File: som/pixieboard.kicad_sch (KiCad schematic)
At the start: 5 parts, among them SW1 SW_DIP_x03, U1 XC7A200T-3FBG484E

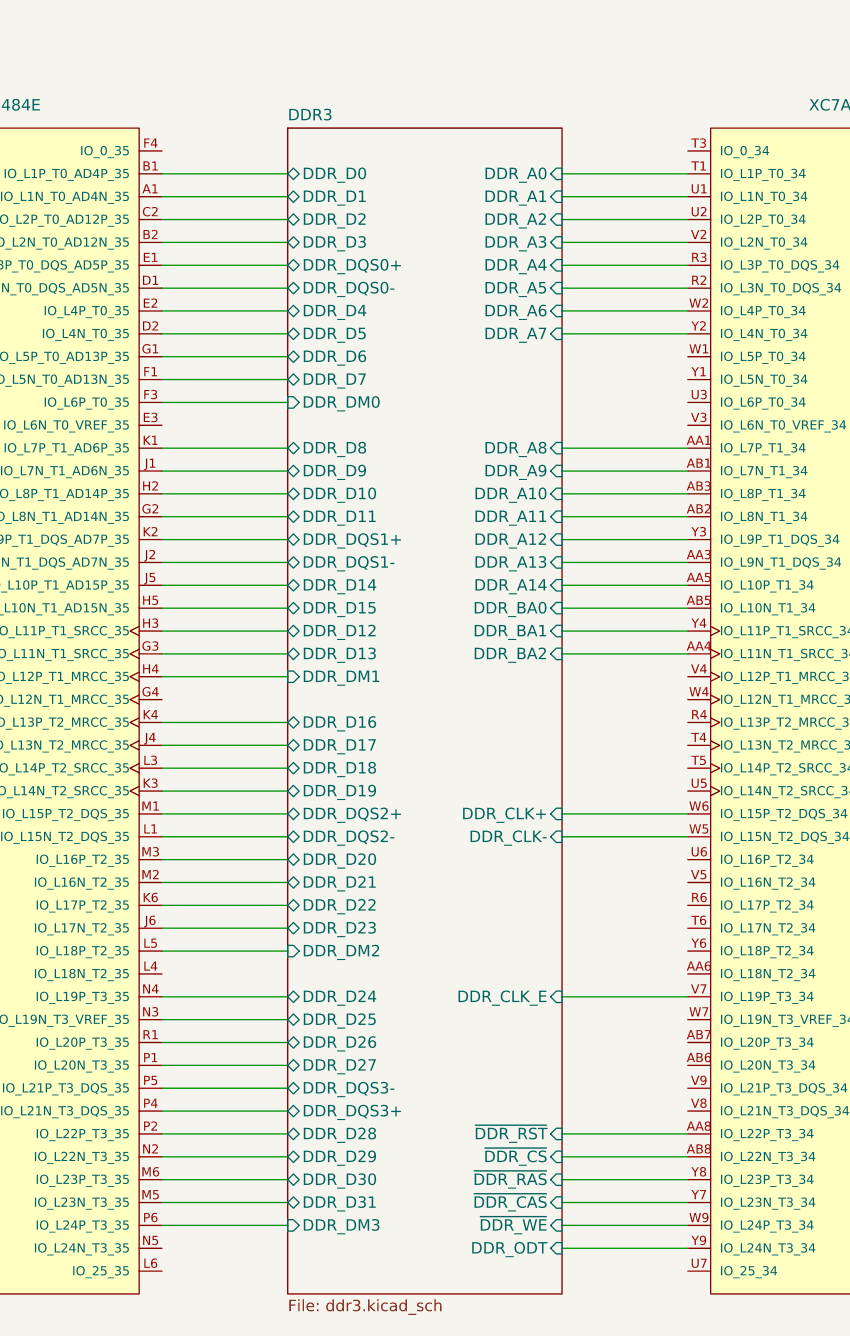
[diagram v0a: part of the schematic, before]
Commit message: Completed DDR3L routing
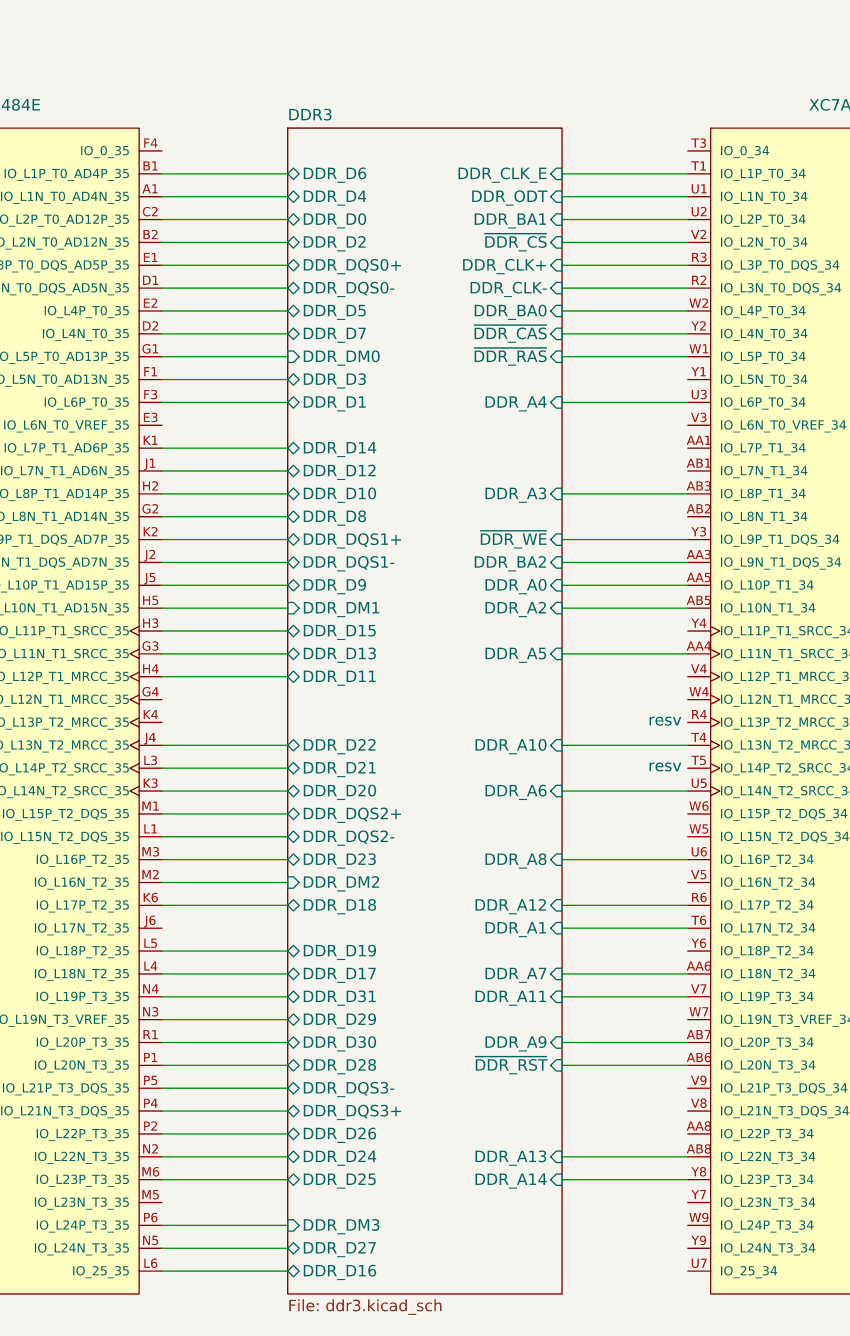
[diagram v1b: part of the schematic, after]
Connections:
- net DDR3/DDR_A0: now also U1.AA5 (IO_L10P_T1_34); no longer U1.T1 (IO_L1P_T0_34)
- net DDR3/DDR_A1: now also U1.T6 (IO_L17N_T2_34); no longer U1.U1 (IO_L1N_T0_34)
- net DDR3/DDR_A10: now also U1.T4 (IO_L13N_T2_MRCC_34); no longer U1.AB3 (IO_L8P_T1_34)
- net DDR3/DDR_A11: now also U1.V7 (IO_L19P_T3_34); no longer U1.AB2 (IO_L8N_T1_34)
- net DDR3/DDR_A12: now also U1.R6 (IO_L17P_T2_34); no longer U1.Y3 (IO_L9P_T1_DQS_34)
- net DDR3/DDR_A13: now also U1.AB8 (IO_L22N_T3_34); no longer U1.AA3 (IO_L9N_T1_DQS_34)
- net DDR3/DDR_A14: now also U1.Y8 (IO_L23P_T3_34); no longer U1.AA5 (IO_L10P_T1_34)
- net DDR3/DDR_A2: now also U1.AB5 (IO_L10N_T1_34); no longer U1.U2 (IO_L2P_T0_34)
- net DDR3/DDR_A3: now also U1.AB3 (IO_L8P_T1_34); no longer U1.V2 (IO_L2N_T0_34)
- net DDR3/DDR_A4: now also U1.U3 (IO_L6P_T0_34); no longer U1.R3 (IO_L3P_T0_DQS_34)
- net DDR3/DDR_A5: now also U1.AA4 (IO_L11N_T1_SRCC_34); no longer U1.R2 (IO_L3N_T0_DQS_34)
- net DDR3/DDR_A6: now also U1.U5 (IO_L14N_T2_SRCC_34); no longer U1.W2 (IO_L4P_T0_34)
- net DDR3/DDR_A7: now also U1.AA6 (IO_L18N_T2_34); no longer U1.Y2 (IO_L4N_T0_34)
- net DDR3/DDR_A8: now also U1.U6 (IO_L16P_T2_34); no longer U1.AA1 (IO_L7P_T1_34)
- net DDR3/DDR_A9: now also U1.AB7 (IO_L20P_T3_34); no longer U1.AB1 (IO_L7N_T1_34)
- net DDR3/DDR_BA0: now also U1.W2 (IO_L4P_T0_34); no longer U1.AB5 (IO_L10N_T1_34)
- net DDR3/DDR_BA1: now also U1.U2 (IO_L2P_T0_34); no longer U1.Y4 (IO_L11P_T1_SRCC_34)
- net DDR3/DDR_BA2: now also U1.AA3 (IO_L9N_T1_DQS_34); no longer U1.AA4 (IO_L11N_T1_SRCC_34)
- net DDR3/DDR_CLK+: now also U1.R3 (IO_L3P_T0_DQS_34); no longer U1.W6 (IO_L15P_T2_DQS_34)
- net DDR3/DDR_CLK-: now also U1.R2 (IO_L3N_T0_DQS_34); no longer U1.W5 (IO_L15N_T2_DQS_34)
- net DDR3/DDR_CLK_E: now also U1.T1 (IO_L1P_T0_34); no longer U1.V7 (IO_L19P_T3_34)
- net DDR3/DDR_D0: now also U1.C2 (IO_L2P_T0_AD12P_35); no longer U1.B1 (IO_L1P_T0_AD4P_35)
- net DDR3/DDR_D1: now also U1.F3 (IO_L6P_T0_35); no longer U1.A1 (IO_L1N_T0_AD4N_35)
- net DDR3/DDR_D11: now also U1.H4 (IO_L12P_T1_MRCC_35); no longer U1.G2 (IO_L8N_T1_AD14N_35)
- net DDR3/DDR_D12: now also U1.J1 (IO_L7N_T1_AD6N_35); no longer U1.H3 (IO_L11P_T1_SRCC_35)
- net DDR3/DDR_D14: now also U1.K1 (IO_L7P_T1_AD6P_35); no longer U1.J5 (IO_L10P_T1_AD15P_35)
- net DDR3/DDR_D15: now also U1.H3 (IO_L11P_T1_SRCC_35); no longer U1.H5 (IO_L10N_T1_AD15N_35)
- net DDR3/DDR_D16: now also U1.L6 (IO_25_35); no longer U1.K4 (IO_L13P_T2_MRCC_35)
- net DDR3/DDR_D17: now also U1.L4 (IO_L18N_T2_35); no longer U1.J4 (IO_L13N_T2_MRCC_35)
- net DDR3/DDR_D18: now also U1.K6 (IO_L17P_T2_35); no longer U1.L3 (IO_L14P_T2_SRCC_35)
- net DDR3/DDR_D19: now also U1.L5 (IO_L18P_T2_35); no longer U1.K3 (IO_L14N_T2_SRCC_35)
- net DDR3/DDR_D2: now also U1.B2 (IO_L2N_T0_AD12N_35); no longer U1.C2 (IO_L2P_T0_AD12P_35)
- net DDR3/DDR_D20: now also U1.K3 (IO_L14N_T2_SRCC_35); no longer U1.M3 (IO_L16P_T2_35)
- net DDR3/DDR_D21: now also U1.L3 (IO_L14P_T2_SRCC_35); no longer U1.M2 (IO_L16N_T2_35)
- net DDR3/DDR_D22: now also U1.J4 (IO_L13N_T2_MRCC_35); no longer U1.K6 (IO_L17P_T2_35)
- net DDR3/DDR_D23: now also U1.M3 (IO_L16P_T2_35); no longer U1.J6 (IO_L17N_T2_35)
- net DDR3/DDR_D24: now also U1.N2 (IO_L22N_T3_35); no longer U1.N4 (IO_L19P_T3_35)
- net DDR3/DDR_D25: now also U1.M6 (IO_L23P_T3_35); no longer U1.N3 (IO_L19N_T3_VREF_35)
- net DDR3/DDR_D26: now also U1.P2 (IO_L22P_T3_35); no longer U1.R1 (IO_L20P_T3_35)
- net DDR3/DDR_D27: now also U1.N5 (IO_L24N_T3_35); no longer U1.P1 (IO_L20N_T3_35)
- net DDR3/DDR_D28: now also U1.P1 (IO_L20N_T3_35); no longer U1.P2 (IO_L22P_T3_35)
- net DDR3/DDR_D29: now also U1.N3 (IO_L19N_T3_VREF_35); no longer U1.N2 (IO_L22N_T3_35)
- net DDR3/DDR_D3: now also U1.F1 (IO_L5N_T0_AD13N_35); no longer U1.B2 (IO_L2N_T0_AD12N_35)
- net DDR3/DDR_D30: now also U1.R1 (IO_L20P_T3_35); no longer U1.M6 (IO_L23P_T3_35)
- net DDR3/DDR_D31: now also U1.N4 (IO_L19P_T3_35); no longer U1.M5 (IO_L23N_T3_35)
- net DDR3/DDR_D4: now also U1.A1 (IO_L1N_T0_AD4N_35); no longer U1.E2 (IO_L4P_T0_35)
- net DDR3/DDR_D5: now also U1.E2 (IO_L4P_T0_35); no longer U1.D2 (IO_L4N_T0_35)
- net DDR3/DDR_D6: now also U1.B1 (IO_L1P_T0_AD4P_35); no longer U1.G1 (IO_L5P_T0_AD13P_35)
- net DDR3/DDR_D7: now also U1.D2 (IO_L4N_T0_35); no longer U1.F1 (IO_L5N_T0_AD13N_35)
- net DDR3/DDR_D8: now also U1.G2 (IO_L8N_T1_AD14N_35); no longer U1.K1 (IO_L7P_T1_AD6P_35)
- net DDR3/DDR_D9: now also U1.J5 (IO_L10P_T1_AD15P_35); no longer U1.J1 (IO_L7N_T1_AD6N_35)
- net DDR3/DDR_DM0: now also U1.G1 (IO_L5P_T0_AD13P_35); no longer U1.F3 (IO_L6P_T0_35)
- net DDR3/DDR_DM1: now also U1.H5 (IO_L10N_T1_AD15N_35); no longer U1.H4 (IO_L12P_T1_MRCC_35)
- net DDR3/DDR_DM2: now also U1.M2 (IO_L16N_T2_35); no longer U1.L5 (IO_L18P_T2_35)
- net DDR3/DDR_ODT: now also U1.U1 (IO_L1N_T0_34); no longer U1.Y9 (IO_L24N_T3_34)
- net DDR3/~{DDR_CAS}: now also U1.Y2 (IO_L4N_T0_34); no longer U1.Y7 (IO_L23N_T3_34)
- net DDR3/~{DDR_CS}: now also U1.V2 (IO_L2N_T0_34); no longer U1.AB8 (IO_L22N_T3_34)
- net DDR3/~{DDR_RAS}: now also U1.W1 (IO_L5P_T0_34); no longer U1.Y8 (IO_L23P_T3_34)
- net DDR3/~{DDR_RST}: now also U1.AB6 (IO_L20N_T3_34); no longer U1.AA8 (IO_L22P_T3_34)
- net DDR3/~{DDR_WE}: now also U1.Y3 (IO_L9P_T1_DQS_34); no longer U1.W9 (IO_L24P_T3_34)
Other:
- note added: "resv"

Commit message: Mezz Power Tweak Ok
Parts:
- added H1, H2, H3, H4: MountingHole_Pad, MountingHole:MountingHole_2.2mm_M2_DIN965_Pad, symbol Mechanical:MountingHole_Pad
- added J1, J2, J3, J4: Conn_02x20_Counter_Clockwise, Mezzanine:Mezz_02x20_p0.5mm_M, symbol Connector_Generic:Conn_02x20_Counter_Clockwise
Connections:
- net GND: now also H1.1, H2.1, H3.1, H4.1

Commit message: Le DDR3 control traces
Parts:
- added C33: 100nF, Capacitor_SMD:C_0402_1005Metric, symbol Device:C_Small
- added J5, J6: Conn_02x20_Counter_Clockwise, Mezzanine:Mezz_02x20_p0.5mm_M, symbol Connector_Generic:Conn_02x20_Counter_Clockwise
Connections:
- net +3V3: now also C33.1
- net DDR3/DDR_A1: now also U1.V5 (IO_L16N_T2_34); no longer U1.T6 (IO_L17N_T2_34)
- net DDR3/DDR_A10: now also U1.T6 (IO_L17N_T2_34); no longer U1.T4 (IO_L13N_T2_MRCC_34)
- net DDR3/DDR_A11: now also U1.W6 (IO_L15P_T2_DQS_34); no longer U1.V7 (IO_L19P_T3_34)
- net DDR3/DDR_A12: now also U1.V4 (IO_L12P_T1_MRCC_34); no longer U1.R6 (IO_L17P_T2_34)
- net DDR3/DDR_A14: now also U1.W7 (IO_L19N_T3_VREF_34); no longer U1.Y8 (IO_L23P_T3_34)
- net DDR3/DDR_A2: now also U1.AA6 (IO_L18N_T2_34); no longer U1.AB5 (IO_L10N_T1_34)
- net DDR3/DDR_A3: now also U1.AA4 (IO_L11N_T1_SRCC_34); no longer U1.AB3 (IO_L8P_T1_34)
- net DDR3/DDR_A4: now also U1.T4 (IO_L13N_T2_MRCC_34); no longer U1.U3 (IO_L6P_T0_34)
- net DDR3/DDR_A5: now also U1.AB5 (IO_L10N_T1_34); no longer U1.AA4 (IO_L11N_T1_SRCC_34)
- net DDR3/DDR_A7: now also U1.AB6 (IO_L20N_T3_34); no longer U1.AA6 (IO_L18N_T2_34)
- net DDR3/DDR_A9: now also U1.Y7 (IO_L23N_T3_34); no longer U1.AB7 (IO_L20P_T3_34)
- net DDR3/DDR_BA0: now also U1.AA3 (IO_L9N_T1_DQS_34); no longer U1.W2 (IO_L4P_T0_34)
- net DDR3/DDR_BA1: now also U1.W2 (IO_L4P_T0_34); no longer U1.U2 (IO_L2P_T0_34)
- net DDR3/DDR_BA2: now also U1.Y4 (IO_L11P_T1_SRCC_34); no longer U1.AA3 (IO_L9N_T1_DQS_34)
- net DDR3/DDR_CLK_E: now also U1.R6 (IO_L17P_T2_34); no longer U1.T1 (IO_L1P_T0_34)
- net DDR3/~{DDR_CAS}: now also U1.U2 (IO_L2P_T0_34); no longer U1.Y2 (IO_L4N_T0_34)
- net DDR3/~{DDR_RAS}: now also U1.T1 (IO_L1P_T0_34); no longer U1.W1 (IO_L5P_T0_34)
- net DDR3/~{DDR_RST}: now also U1.AB7 (IO_L20P_T3_34); no longer U1.AB6 (IO_L20N_T3_34)
- net GND: now also C33.2
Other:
- moved on the sheet: U1G

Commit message: ok
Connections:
- net DDR3/DDR_A0: no longer U1.AA5 (IO_L10P_T1_34)
- net DDR3/DDR_A1: no longer U1.V5 (IO_L16N_T2_34)
- net DDR3/DDR_A10: now also U1.U3 (IO_L6P_T0_34); no longer U1.T6 (IO_L17N_T2_34)
- net DDR3/DDR_A11: no longer U1.W6 (IO_L15P_T2_DQS_34)
- net DDR3/DDR_A13: no longer U1.AB8 (IO_L22N_T3_34)
- net DDR3/DDR_A14: no longer U1.W7 (IO_L19N_T3_VREF_34)
- net DDR3/DDR_A2: no longer U1.AA6 (IO_L18N_T2_34)
- net DDR3/DDR_A3: no longer U1.AA4 (IO_L11N_T1_SRCC_34)
- net DDR3/DDR_A4: now also U1.Y6 (IO_L18P_T2_34); no longer U1.T4 (IO_L13N_T2_MRCC_34)
- net DDR3/DDR_A5: no longer U1.AB5 (IO_L10N_T1_34)
- net DDR3/DDR_A6: now also U1.AA6 (IO_L18N_T2_34); no longer U1.U5 (IO_L14N_T2_SRCC_34)
- net DDR3/DDR_A7: no longer U1.AB6 (IO_L20N_T3_34)
- net DDR3/DDR_A8: now also U1.AB7 (IO_L20P_T3_34); no longer U1.U6 (IO_L16P_T2_34)
- net DDR3/DDR_A9: no longer U1.Y7 (IO_L23N_T3_34)
- net DDR3/DDR_BA0: no longer U1.AA3 (IO_L9N_T1_DQS_34)
- net DDR3/DDR_BA1: now also U1.W5 (IO_L15N_T2_DQS_34); no longer U1.W2 (IO_L4P_T0_34)
- net DDR3/DDR_BA2: no longer U1.Y4 (IO_L11P_T1_SRCC_34)
- net DDR3/DDR_CLK+: now also U1.T1 (IO_L1P_T0_34); no longer U1.R3 (IO_L3P_T0_DQS_34)
- net DDR3/DDR_CLK-: now also U1.U1 (IO_L1N_T0_34); no longer U1.R2 (IO_L3N_T0_DQS_34)
- net DDR3/DDR_CLK_E: now also U1.U2 (IO_L2P_T0_34); no longer U1.R6 (IO_L17P_T2_34)
- net DDR3/DDR_ODT: no longer U1.U1 (IO_L1N_T0_34)
- net DDR3/~{DDR_CAS}: no longer U1.U2 (IO_L2P_T0_34)
- net DDR3/~{DDR_CS}: no longer U1.V2 (IO_L2N_T0_34)
- net DDR3/~{DDR_RAS}: no longer U1.T1 (IO_L1P_T0_34)
- net DDR3/~{DDR_RST}: no longer U1.AB7 (IO_L20P_T3_34)
- net DDR3/~{DDR_WE}: no longer U1.Y3 (IO_L9P_T1_DQS_34)

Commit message: DDR3 (again)
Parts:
- added C53, C54, C55, C56: 1nF, Capacitor_SMD:C_0402_1005Metric, symbol Device:C_Small
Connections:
- net DDR3/DDR_A0: now also U1.W5 (IO_L15N_T2_DQS_34)
- net DDR3/DDR_A1: now also U1.W4 (IO_L12N_T1_MRCC_34)
- net DDR3/DDR_A10: now also U1.R6 (IO_L17P_T2_34); no longer U1.U3 (IO_L6P_T0_34)
- net DDR3/DDR_A11: now also U1.Y6 (IO_L18P_T2_34)
- net DDR3/DDR_A12: now also U1.T6 (IO_L17N_T2_34); no longer U1.V4 (IO_L12P_T1_MRCC_34)
- net DDR3/DDR_A13: now also U1.AB6 (IO_L20N_T3_34)
- net DDR3/DDR_A14: now also U1.AB7 (IO_L20P_T3_34)
- net DDR3/DDR_A2: now also U1.AA5 (IO_L10P_T1_34)
- net DDR3/DDR_A3: now also U1.Y3 (IO_L9P_T1_DQS_34)
- net DDR3/DDR_A4: now also U1.V7 (IO_L19P_T3_34); no longer U1.Y6 (IO_L18P_T2_34)
- net DDR3/DDR_A5: now also U1.Y4 (IO_L11P_T1_SRCC_34)
- net DDR3/DDR_A6: now also U1.Y7 (IO_L23N_T3_34); no longer U1.AA6 (IO_L18N_T2_34)
- net DDR3/DDR_A7: now also U1.AA4 (IO_L11N_T1_SRCC_34)
- net DDR3/DDR_A8: now also U1.AA8 (IO_L22P_T3_34); no longer U1.AB7 (IO_L20P_T3_34)
- net DDR3/DDR_A9: now also U1.AB5 (IO_L10N_T1_34)
- net DDR3/DDR_BA0: now also U1.Y2 (IO_L4N_T0_34)
- net DDR3/DDR_BA1: now also U1.U6 (IO_L16P_T2_34); no longer U1.W5 (IO_L15N_T2_DQS_34)
- net DDR3/DDR_BA2: now also U1.V4 (IO_L12P_T1_MRCC_34)
- net DDR3/DDR_CLK_E: now also U1.R3 (IO_L3P_T0_DQS_34); no longer U1.U2 (IO_L2P_T0_34)
- net DDR3/DDR_D1: now also U1.G1 (IO_L5P_T0_AD13P_35); no longer U1.F3 (IO_L6P_T0_35)
- net DDR3/DDR_D10: now also U1.K1 (IO_L7P_T1_AD6P_35); no longer U1.H2 (IO_L8P_T1_AD14P_35)
- net DDR3/DDR_D11: now also U1.G3 (IO_L11N_T1_SRCC_35); no longer U1.H4 (IO_L12P_T1_MRCC_35)
- net DDR3/DDR_D12: now also U1.H4 (IO_L12P_T1_MRCC_35); no longer U1.J1 (IO_L7N_T1_AD6N_35)
- net DDR3/DDR_D13: now also U1.H5 (IO_L10N_T1_AD15N_35); no longer U1.G3 (IO_L11N_T1_SRCC_35)
- net DDR3/DDR_D14: now also U1.H2 (IO_L8P_T1_AD14P_35); no longer U1.K1 (IO_L7P_T1_AD6P_35)
- net DDR3/DDR_D15: now also U1.G4 (IO_L12N_T1_MRCC_35); no longer U1.H3 (IO_L11P_T1_SRCC_35)
- net DDR3/DDR_D16: now also U1.M2 (IO_L16N_T2_35); no longer U1.L6 (IO_25_35)
- net DDR3/DDR_D18: now also U1.L3 (IO_L14P_T2_SRCC_35); no longer U1.K6 (IO_L17P_T2_35)
- net DDR3/DDR_D2: now also U1.B1 (IO_L1P_T0_AD4P_35); no longer U1.B2 (IO_L2N_T0_AD12N_35)
- net DDR3/DDR_D20: now also U1.J4 (IO_L13N_T2_MRCC_35); no longer U1.K3 (IO_L14N_T2_SRCC_35)
- net DDR3/DDR_D21: now also U1.M3 (IO_L16P_T2_35); no longer U1.L3 (IO_L14P_T2_SRCC_35)
- net DDR3/DDR_D22: now also U1.K3 (IO_L14N_T2_SRCC_35); no longer U1.J4 (IO_L13N_T2_MRCC_35)
- net DDR3/DDR_D23: now also U1.K4 (IO_L13P_T2_MRCC_35); no longer U1.M3 (IO_L16P_T2_35)
- net DDR3/DDR_D24: now also U1.P2 (IO_L22P_T3_35); no longer U1.N2 (IO_L22N_T3_35)
- net DDR3/DDR_D25: now also U1.N2 (IO_L22N_T3_35); no longer U1.M6 (IO_L23P_T3_35)
- net DDR3/DDR_D26: now also U1.R1 (IO_L20P_T3_35); no longer U1.P2 (IO_L22P_T3_35)
- net DDR3/DDR_D27: now also U1.N4 (IO_L19P_T3_35); no longer U1.N5 (IO_L24N_T3_35)
- net DDR3/DDR_D28: now also U1.M6 (IO_L23P_T3_35); no longer U1.P1 (IO_L20N_T3_35)
- net DDR3/DDR_D29: now also U1.P1 (IO_L20N_T3_35); no longer U1.N3 (IO_L19N_T3_VREF_35)
- net DDR3/DDR_D3: now also U1.F3 (IO_L6P_T0_35); no longer U1.F1 (IO_L5N_T0_AD13N_35)
- net DDR3/DDR_D30: now also U1.P6 (IO_L24P_T3_35); no longer U1.R1 (IO_L20P_T3_35)
- net DDR3/DDR_D31: now also U1.N5 (IO_L24N_T3_35); no longer U1.N4 (IO_L19P_T3_35)
- net DDR3/DDR_D5: now also U1.F1 (IO_L5N_T0_AD13N_35); no longer U1.E2 (IO_L4P_T0_35)
- net DDR3/DDR_D6: now also U1.B2 (IO_L2N_T0_AD12N_35); no longer U1.B1 (IO_L1P_T0_AD4P_35)
- net DDR3/DDR_D8: now also U1.J1 (IO_L7N_T1_AD6N_35); no longer U1.G2 (IO_L8N_T1_AD14N_35)
- net DDR3/DDR_D9: now also U1.H3 (IO_L11P_T1_SRCC_35); no longer U1.J5 (IO_L10P_T1_AD15P_35)
- net DDR3/DDR_DM0: now also U1.E2 (IO_L4P_T0_35); no longer U1.G1 (IO_L5P_T0_AD13P_35)
- net DDR3/DDR_DM1: now also U1.G2 (IO_L8N_T1_AD14N_35); no longer U1.H5 (IO_L10N_T1_AD15N_35)
- net DDR3/DDR_DM2: now also U1.K6 (IO_L17P_T2_35); no longer U1.M2 (IO_L16N_T2_35)
- net DDR3/DDR_DM3: now also U1.M5 (IO_L23N_T3_35); no longer U1.P6 (IO_L24P_T3_35)
- net DDR3/DDR_ODT: now also U1.W1 (IO_L5P_T0_34)
- net DDR3/~{DDR_CAS}: now also U1.U3 (IO_L6P_T0_34)
- net DDR3/~{DDR_CS}: now also U1.W2 (IO_L4P_T0_34)
- net DDR3/~{DDR_RAS}: now also U1.U2 (IO_L2P_T0_34)
- net DDR3/~{DDR_WE}: now also U1.V2 (IO_L2N_T0_34)
- net GND: now also C53.2, C54.2, C55.2, C56.2
- net DDR_VREF: now reaches U1.V3 (IO_L6N_T0_VREF_34)
- net DDR_VREF: now also U1.E3 (IO_L6N_T0_VREF_35), U1.N3 (IO_L19N_T3_VREF_35), U1.W7 (IO_L19N_T3_VREF_34), C53.1, C54.1, C55.1, C56.1
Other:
- sheet DDR3 ports: added DDR_VREF; removed none
- note added: "Power rail summary: - 3.3 v 5.0 A input - 1.8 v 1.0 A output - 1.35 v 1.0 A output - 1.2 v 1.0 A output - 1.0 v 10.0 A local"

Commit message: I really should commit when I make it and not a month later
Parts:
- added C57: 100nF, Capacitor_SMD:C_0402_1005Metric, symbol Device:C_Small
- added U4: W25Q128JVS, Package_SO:SOIC-8_5.23x5.23mm_P1.27mm, symbol Memory_Flash:W25Q128JVS
- J1, J2, J3, J4, J5, J6: footprint Mezzanine:Mezz_02x20_p0.5mm_M -> Mezzanine:YXT-BB10-40P-02
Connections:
- net +3V3: now also C57.1, U4.8 (VCC)
- net GND: now also J1.35 (Pin_35), J1.36 (Pin_36), J1.37 (Pin_37), J1.4 (Pin_4), J1.5 (Pin_5), J1.6 (Pin_6), U1.L9 (VREFN_0), U1.M10 (VREFP_0), C57.2, U4.4 (GND)
- net QPI_CCLK: now also U4.6 (CLK)
- net QPI_CS: now also U4.1 (~{CS})
- net QPI_D0: now also U4.5 (DI(IO0))
- net QPI_D1: now also U4.2 (DO(IO1))
- net QPI_D2: now also U4.3 (IO2)
- net QPI_D3: now also U4.7 (IO3)
- net +5V: now reaches J1.1 (Pin_1)
- net +5V: now also J1.2 (Pin_2), J1.3 (Pin_3), J1.38 (Pin_38), J1.39 (Pin_39), J1.40 (Pin_40)
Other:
- sheet Power ports: added P_{GOOD}, V_{in}; removed none
- note removed: "Power rail summary: - 3.3 v 5.0 A input - 1.8 v 1.0 A output - 1.35 v 1.0 A output - 1.2 v 1.0 A output - 1.0 v 10.0 A local"
- moved on the sheet: J1

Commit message: ok
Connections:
- net +3V3: now also J1.33 (Pin_33), J1.34 (Pin_34), J1.7 (Pin_7), J1.8 (Pin_8)
- net GND: now also J1.32 (Pin_32), J1.9 (Pin_9)

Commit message: Work on GTP and power supplies for it
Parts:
- added R19: 240R, Resistor_SMD:R_0402_1005Metric, symbol Device:R_Small
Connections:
- net GND: now also J1.11 (Pin_11), J1.14 (Pin_14), J1.17 (Pin_17), J1.20 (Pin_20), J1.21 (Pin_21), J1.24 (Pin_24), J1.27 (Pin_27), J1.30 (Pin_30), J2.1 (Pin_1), J2.10 (Pin_10), J2.13 (Pin_13), J2.16 (Pin_16), J2.19 (Pin_19), J2.20 (Pin_20), J2.21 (Pin_21), J2.22 (Pin_22), J2.25 (Pin_25), J2.28 (Pin_28), J2.31 (Pin_31), J2.34 (Pin_34), J2.37 (Pin_37), J2.4 (Pin_4), J2.40 (Pin_40), J2.7 (Pin_7); no longer J1.32 (Pin_32), J1.9 (Pin_9)
- net MGT_TX0-: now reaches J1.10 (Pin_10)
- net MGT_TX0-: now also J1.31 (Pin_31), U1.A4 (MGTPTXN0_216)
- net MGT_TX1+: now reaches J1.12 (Pin_12)
- net MGT_TX1+: now also J1.29 (Pin_29), U1.D5 (MGTPTXP1_216)
- net MGT_TX1-: now reaches J1.13 (Pin_13)
- net MGT_TX1-: now also J1.28 (Pin_28), U1.C5 (MGTPTXN1_216)
- net MGT_TX2+: now reaches J1.15 (Pin_15)
- net MGT_TX2+: now also J1.26 (Pin_26), U1.B6 (MGTPTXP2_216)
- net MGT_TX2-: now reaches J1.16 (Pin_16)
- net MGT_TX2-: now also J1.25 (Pin_25), U1.A6 (MGTPTXN2_216)
- net MGT_TX3+: now reaches J1.18 (Pin_18)
- net MGT_TX3+: now also J1.23 (Pin_23), U1.D7 (MGTPTXP3_216)
- net MGT_TX3-: now reaches J1.19 (Pin_19)
- net MGT_TX3-: now also J1.22 (Pin_22), U1.C7 (MGTPTXN3_216)
- net MGT_RX2-: now reaches U1.A10 (MGTPRXN2_216)
- net MGT_RX2-: now also J2.15 (Pin_15), J2.26 (Pin_26)
- net MGT_RX0-: now reaches U1.A8 (MGTPRXN0_216)
- net MGT_RX0-: now also J2.32 (Pin_32), J2.9 (Pin_9)
- net MGT_RX2+: now reaches U1.B10 (MGTPRXP2_216)
- net MGT_RX2+: now also J2.14 (Pin_14), J2.27 (Pin_27)
- net MGT_TX0+: now reaches U1.B4 (MGTPTXP0_216)
- net MGT_TX0+: now also J1.32 (Pin_32), J1.9 (Pin_9)
- net MGT_RX0+: now reaches U1.B8 (MGTPRXP0_216)
- net MGT_RX0+: now also J2.33 (Pin_33), J2.8 (Pin_8)
- net MGT_RX1-: now reaches U1.C11 (MGTPRXN1_216)
- net MGT_RX1-: now also J2.12 (Pin_12), J2.29 (Pin_29)
- net MGT_RX3-: now reaches U1.C9 (MGTPRXN3_216)
- net MGT_RX3-: now also J2.18 (Pin_18), J2.23 (Pin_23)
- net MGT_RX1+: now reaches U1.D11 (MGTPRXP1_216)
- net MGT_RX1+: now also J2.11 (Pin_11), J2.30 (Pin_30)
- net MGT_RX3+: now reaches U1.D9 (MGTPRXP3_216)
- net MGT_RX3+: now also J2.17 (Pin_17), J2.24 (Pin_24)
- net MGT_REF1-: now reaches U1.E10 (MGTREFCLK1N_216)
- net MGT_REF1-: now also J2.35 (Pin_35), J2.6 (Pin_6)
- net MGT_REF0-: now reaches U1.E6 (MGTREFCLK0N_216)
- net MGT_REF0-: now also J2.3 (Pin_3), J2.38 (Pin_38)
- net MGT_REF1+: now reaches U1.F10 (MGTREFCLK1P_216)
- net MGT_REF1+: now also J2.36 (Pin_36), J2.5 (Pin_5)
- net MGT_REF0+: now reaches U1.F6 (MGTREFCLK0P_216)
- net MGT_REF0+: now also J2.2 (Pin_2), J2.39 (Pin_39)
- net at U1.F8 (MGTRREF_216): now also R19.2
- new net +1V2: R19.1
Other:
- note added: "TODO: off-board FLASH and MODESEL to carrier board"
- moved on the sheet: J1, J2, U1H
